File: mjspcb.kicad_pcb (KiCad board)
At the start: 2 copper layers, 83.3 x 40.1 mm, 77 parts, among them P1 3xAAA battery, P1** 2.7 - 6.0 VDC, P2 GND GND Vin RxD TxD RST, P3 HTU21D, P4 GPS, P5 rain, P6 light, P7 moist, P8 perfboard breakout, Q1 STU60N3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

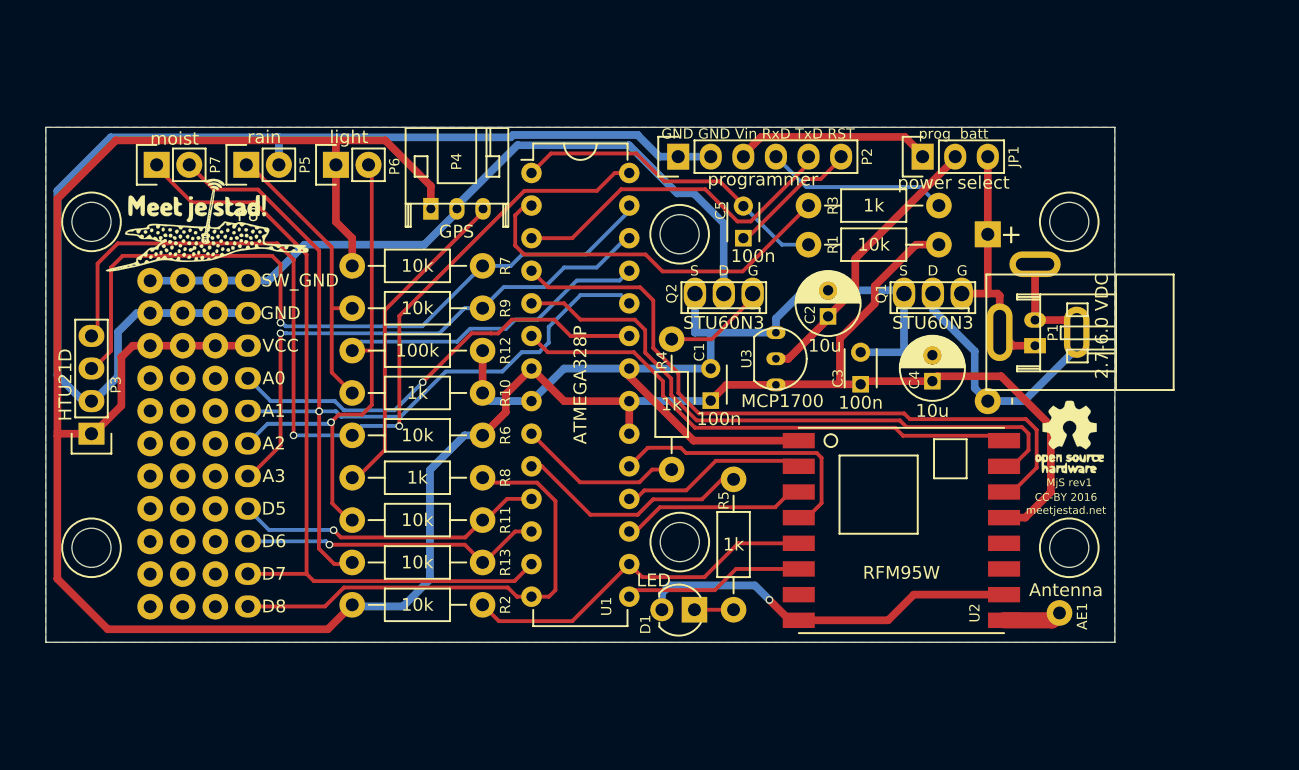
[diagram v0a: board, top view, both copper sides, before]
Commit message: Revision 2 of Meet je stad PCB
*added reset header
*changed pinout of I2C breakout to accomodate Sparkfun Si7021
*various minor other modifications
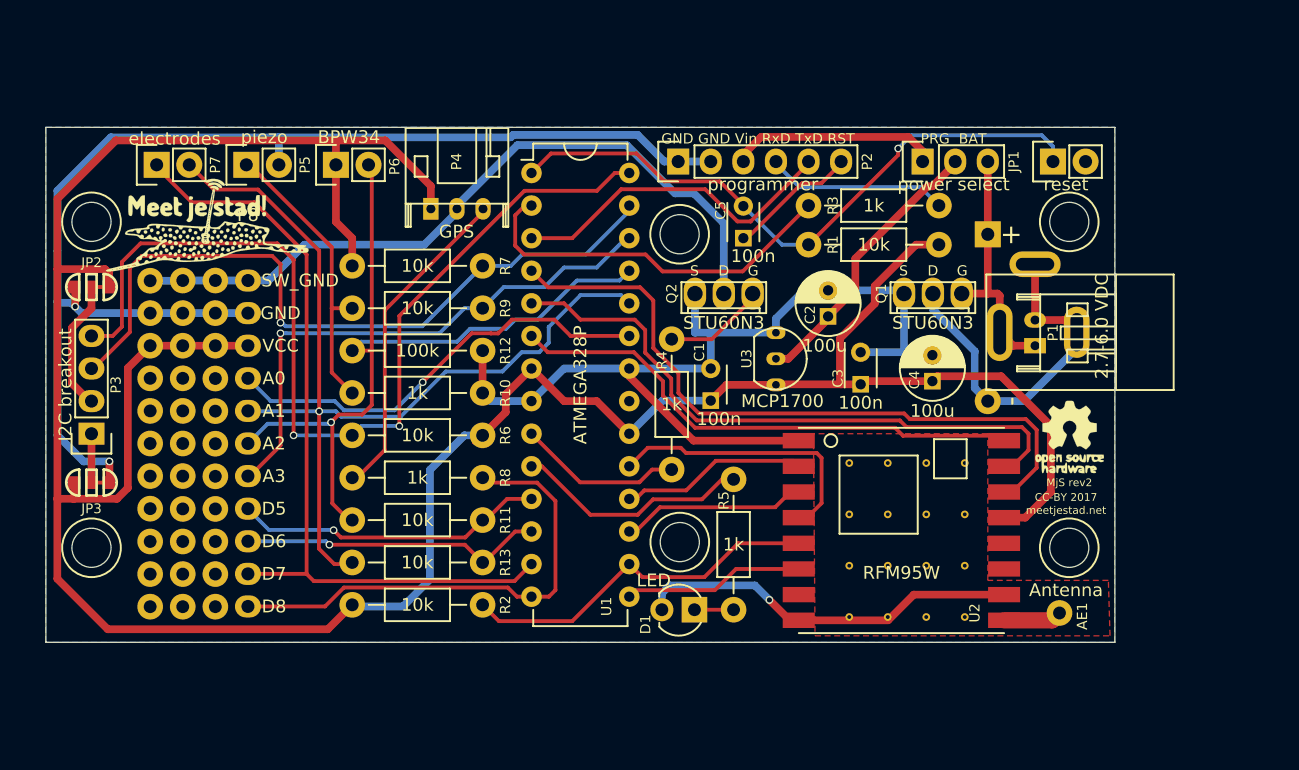
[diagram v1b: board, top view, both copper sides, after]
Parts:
- added JP2: V1, meetjestad:SOLDER-JUMPER_2-WAY-CLOSED, F.Cu at (139.7, 113.0)
- added JP3: V2, meetjestad:SOLDER-JUMPER_2-WAY-CLOSED, F.Cu at (139.7, 128.3)
- added P9: reset, meetjestad:Socket_Strip_Straight_1x02, F.Cu at (214.6, 103.3)
- added REF**: via-0.6mm, meetjestad:via-0.6mm, F.Cu at (207.8, 138.7)
- added REF**: via-0.6mm, meetjestad:via-0.6mm, F.Cu at (204.8, 130.7)
- added REF**: via-0.6mm, meetjestad:via-0.6mm, F.Cu at (201.8, 130.7)
- added REF**: via-0.6mm, meetjestad:via-0.6mm, F.Cu at (198.8, 130.7)
- added REF**: via-0.6mm, meetjestad:via-0.6mm, F.Cu at (207.8, 126.7)
- added REF**: via-0.6mm, meetjestad:via-0.6mm, F.Cu at (204.8, 126.7)
- added REF**: via-0.6mm, meetjestad:via-0.6mm, F.Cu at (201.8, 126.7)
- added REF**: via-0.6mm, meetjestad:via-0.6mm, F.Cu at (198.8, 126.7)
- added REF**: via-0.6mm, meetjestad:via-0.6mm, F.Cu at (204.8, 138.7)
- added REF**: via-0.6mm, meetjestad:via-0.6mm, F.Cu at (201.8, 138.7)
- added REF**: via-0.6mm, meetjestad:via-0.6mm, F.Cu at (198.8, 138.7)
- added REF**: via-0.6mm, meetjestad:via-0.6mm, F.Cu at (207.8, 134.7)
- added REF**: via-0.6mm, meetjestad:via-0.6mm, F.Cu at (204.8, 134.7)
- added REF**: via-0.6mm, meetjestad:via-0.6mm, F.Cu at (201.8, 134.7)
- added REF**: via-0.6mm, meetjestad:via-0.6mm, F.Cu at (198.8, 134.7)
- added REF**: via-0.6mm, meetjestad:via-0.6mm, F.Cu at (207.8, 130.7)
- C2, C4: value 10u -> 100u
- JP1: value prog batt -> PRG BAT
- P1: value 3xAAA battery -> 2.7 - 6.0 VDC
- P3: value HTU21D -> I2C breakout
- P5: value rain -> piezo
- P6: value light -> BPW34
- P7: value moist -> electrodes
- moved JP1 0.38 mm to (204.5, 103.3)
- moved P2 0.38 mm to (185.4, 103.3)
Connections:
- P3 pad 1: VCC -> GND
- P3 pad 2: GND -> VCC
- U1 pad 21: VCC -> Net-(U1-Pad21)
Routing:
- net RST: track 25.4 -> 49.9 mm, vias 0 -> 1
- net VCC: track 221.7 -> 244.6 mm
- net GND: track 195.0 -> 208.6 mm, vias 1 -> 3
- net Net-(JP1-Pad3): track 22.3 -> 21.0 mm
- net Net-(C2-Pad1): track 22.5 -> 21.6 mm
- net SDA: track 58.6 -> 57.7 mm
- added copper zone on F.Cu, net GND
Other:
- board text added: "CC-BY 2017"
- board text added: "MjS rev2"
- board text removed: "CC-BY 2016"
- board text removed: "MjS rev1"

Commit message: Add DC plug and Lipo connector to schematic
These were in the board layout, but not in the schematic. This adds them
to the schematic, and sets the appropriate references in the layouted
footprints.

Note that the DC plug symbol has a different pin numbering than the
footprint currently in use, but the symbol does match the footprint set
in the schematic, so this should work out when the netlist is re-read in
the future.
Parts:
- renumbered DC to DC1, P1** to P10
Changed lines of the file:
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@@
     (at 213.233 116.60124 90)
     (descr "JST PH series connector, S2B-PH-KL")
-    (fp_text reference P1** (at 3.31724 3.302 90) (layer F.SilkS) hide
+    (fp_text reference P10 (at 3.31724 3.302 90) (layer F.SilkS) hide
       (effects (font (size 0.8 0.8) (thickness 0.1)))
     )
@@
     (at 216.73312 116.55298 90)
     (descr "Socket, DC power supply")
-    (fp_text reference DC (at 0 6.27888 90) (layer F.SilkS) hide
+    (fp_text reference DC1 (at 0 6.27888 90) (layer F.SilkS) hide
       (effects (font (size 1 1) (thickness 0.15)))
     )

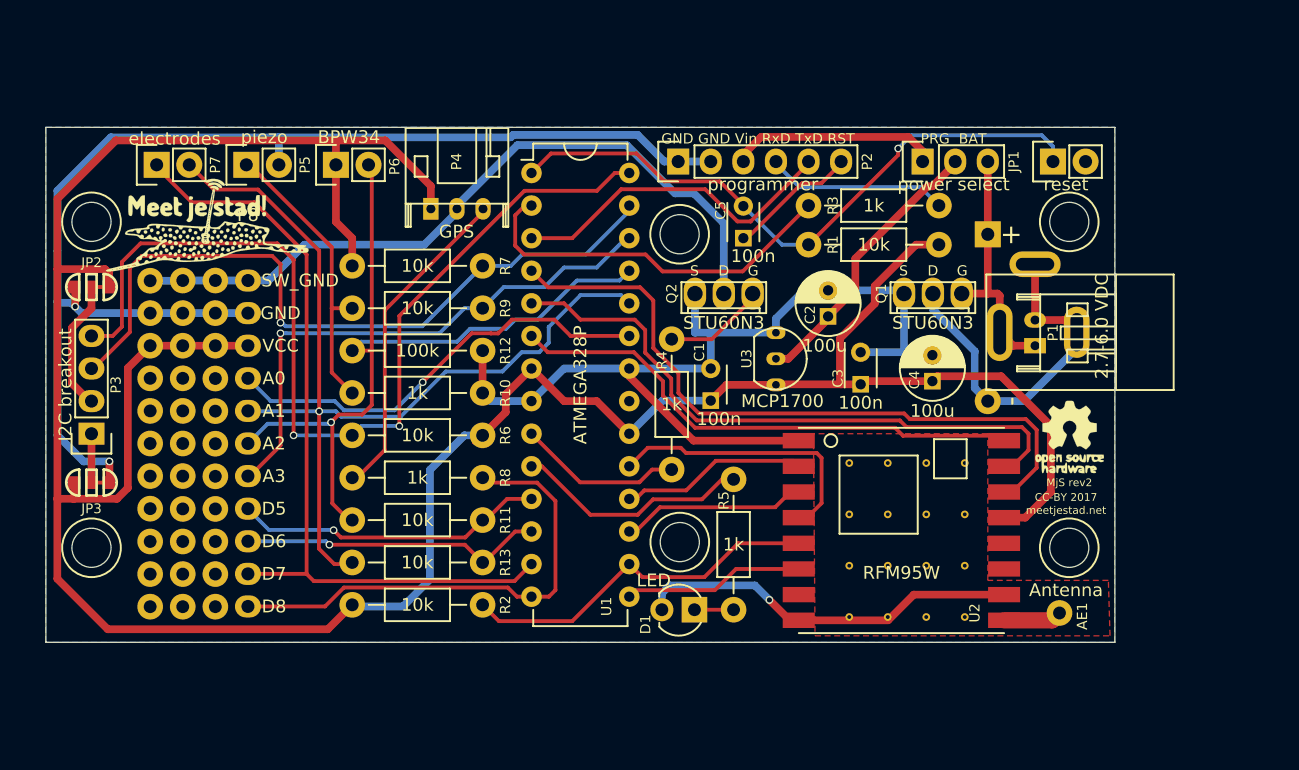
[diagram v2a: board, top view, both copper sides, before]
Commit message: Convert board layout to KiCad 5
This replaces all footprints with new versions from KiCad 5. Some
positions and labeling as changed, so this updates everything to match
the original layout for the most part. Some footprints (barrel jack,
regulator, battery holder, solder jumpers, perfboard "connector") are
slightly different. In particualr the battery holde slightly changes the
mounting hole position and size, so this might need to be changed back
later.

The only footprints that are still used from the project library are the
logo, all others are removed. All components are also in the schematic,
except for the perfboard individiual pins (which also do not have any
external footprint they refer to).

The GPS connector footprint has holes that are slightly (0.05mm) bigger,
which should make it easier to fit the connector.
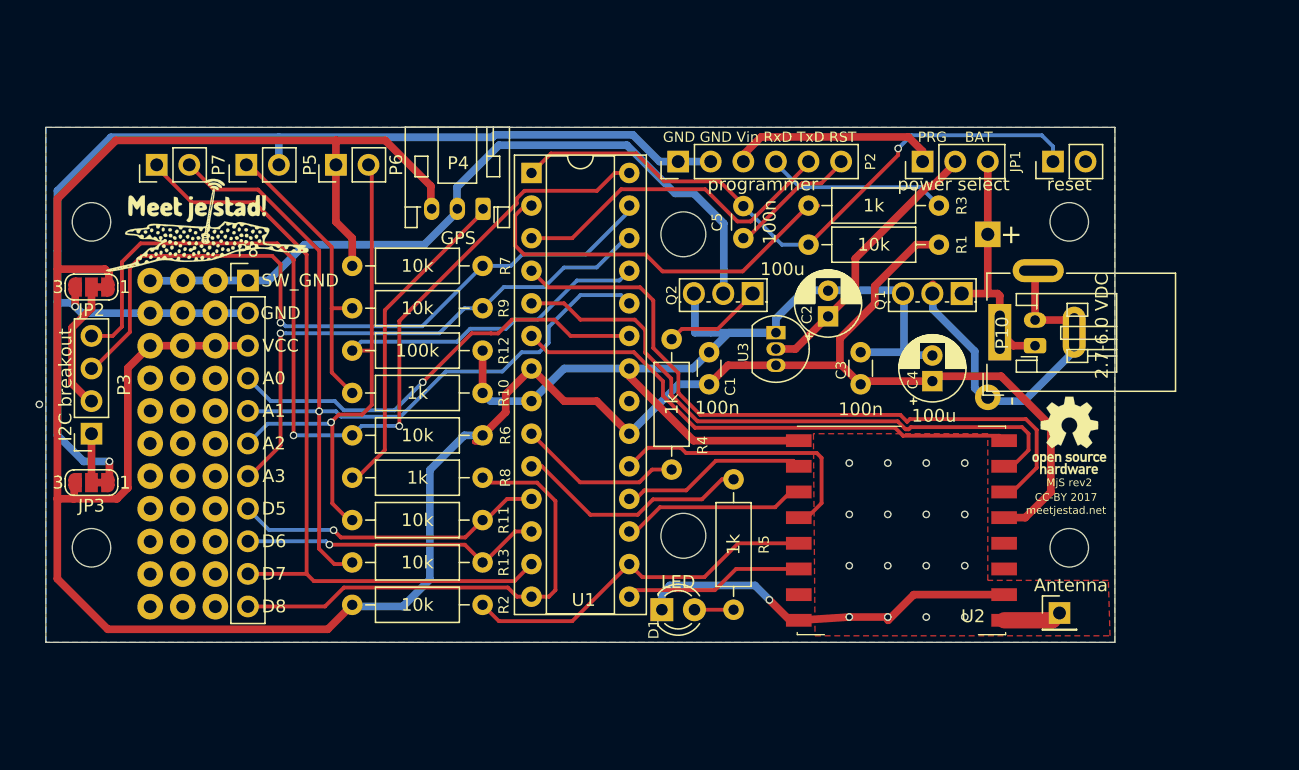
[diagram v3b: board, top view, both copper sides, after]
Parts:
- removed the ? at (185.5, 132.9)
- removed the ? at (185.5, 108.9)
- removed REF** (x16): via-0.6mm, meetjestad:via-0.6mm
- AE1: footprint meetjestad:1pin -> Connector_PinHeader_2.54mm:PinHeader_1x01_P2.54mm_Vertical
- C1, C3, C5: footprint meetjestad:C_Disc_D3_P2.5 -> Capacitor_THT:C_Disc_D3.0mm_W1.6mm_P2.50mm
- C2: footprint meetjestad:C_Radial_D5_L11_P2 -> Capacitor_THT:CP_Radial_D5.0mm_P2.00mm
- C4: footprint C_Radial_D5_L11_P2 -> Capacitor_THT:CP_Radial_D5.0mm_P2.00mm
- D1: footprint LED-3MM -> LED_THT:LED_D3.0mm
- DC1: value P1* -> 2.7 - 6.0 VDC; footprint dc_socket -> Connector_BarrelJack:BarrelJack_Wuerth_6941xx301002
- H1, H2, H3, H4: renamed from ?; value (none) -> MountingHole; footprint Connect:1pin -> MountingHole:MountingHole_3mm
- JP1: value PRG BAT -> power select; footprint meetjestad:Pin_Header_Straight_1x03 -> Connector_PinHeader_2.54mm:PinHeader_1x03_P2.54mm_Vertical
- JP2, JP3: footprint meetjestad:SOLDER-JUMPER_2-WAY-CLOSED -> Jumper:SolderJumper-3_P1.3mm_Bridged12_RoundedPad1.0x1.5mm_NumberLabels
- LOGO1: renamed from G2; value OSHW logo -> Open source hardware; footprint meetjestad:oshw -> Symbol:OSHW-Logo_5.7x6mm_SilkScreen
- LOGO2: renamed from G1; value MjS logo -> MJS Logo
- P1: value 2.7 - 6.0 VDC -> Batteries; footprint Batterypack3xAAA -> Battery:BatteryHolder_Keystone_2479_3xAAA
- P10: value 2.7 - 6.0 VDC -> Lipo; footprint s2b-ph-kl -> Connector_JST:JST_PH_S2B-PH-K_1x02_P2.00mm_Horizontal
- P2: value GND GND Vin RxD TxD RST -> serial breakout; footprint meetjestad:Pin_Header_Straight_1x06 -> Connector_PinHeader_2.54mm:PinHeader_1x06_P2.54mm_Vertical
- P3: footprint meetjestad:Socket_Strip_Straight_1x04 -> Connector_PinSocket_2.54mm:PinSocket_1x04_P2.54mm_Vertical
- P4: footprint s3b-ph-kl -> Connector_JST:JST_PH_S3B-PH-K_1x03_P2.00mm_Horizontal
- P5, P6, P7, P9: footprint meetjestad:Socket_Strip_Straight_1x02 -> Connector_PinHeader_2.54mm:PinHeader_1x02_P2.54mm_Vertical
- P8: footprint Perf_board_connecttion_1x11 -> Connector_PinHeader_2.54mm:PinHeader_1x11_P2.54mm_Vertical
- Q1, Q2: value STU60N3 -> STU60N3LH5; footprint meetjestad:ipak_std -> Package_TO_SOT_THT:TO-251-3_Vertical
- R1, R10, R11, R12, R13, R2, R3, R4, R5, R6, R7, R8, R9: footprint meetjestad:Resistor_Horizontal_RM10mm -> Resistor_THT:R_Axial_DIN0207_L6.3mm_D2.5mm_P10.16mm_Horizontal
- U1: footprint meetjestad:DIP-28_W7.62mm -> Package_DIP:DIP-28_W7.62mm_Socket
- U2: footprint RFM95W -> RF_Module:HOPERF_RFM9XW_SMD
- U3: value MCP1700 -> MCP1700-3302; footprint TO-92_Inline_Narrow_Oval -> Package_TO_SOT_THT:TO-92_Inline
- moved P1 31.1 mm to (209.6, 108.9)
- moved DC1 6.25 mm to (210.5, 116.6)
- moved R1 5.08 mm to (205.7, 109.7)
- moved R3 5.08 mm to (205.7, 106.7)
- moved R4 5.08 mm to (184.9, 117.1)
- moved R5 5.08 mm to (189.7, 128.0)
- moved R6 5.08 mm to (170.2, 124.6)
- moved R10 5.08 mm to (160.0, 121.3)
- moved R11 5.08 mm to (160.0, 131.2)
- moved R12 5.08 mm to (160.0, 118.0)
- moved R13 5.08 mm to (160.0, 134.5)
- moved R2 5.08 mm to (160.0, 137.8)
- moved R7 5.08 mm to (160.0, 111.4)
- moved R8 5.08 mm to (160.0, 127.9)
- moved R9 5.08 mm to (160.0, 114.7)
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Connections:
- net Net-(C2-Pad1) renamed VIN
- net Net-(R2-Pad2) renamed D10
- net Net-(U1-Pad15) renamed D9
- net Net-(U1-Pad17) renamed MOSI
- net Net-(U1-Pad18) renamed MISO
- net Net-(U1-Pad19) renamed SCK
- net Net-(U1-Pad4) renamed D2
- net Net-(U1-Pad5) renamed D3
- net Net-(U1-Pad6) renamed D4
- DC1 pad 1: Net-(P1-Pad1) -> +BATT
- DC1 pad 2: Net-(P1-Pad1) -> -BATT
- DC1 pad 3: Net-(JP1-Pad3) -> -BATT
- JP1 pad 3: Net-(JP1-Pad3) -> +BATT
- JP2 pad 2: GND -> Net-(JP2-Pad2)
- JP3 pad 2: VCC -> Net-(JP3-Pad2)
- P1 pad 1: Net-(P1-Pad1) -> +BATT
- P1 pad 2: Net-(JP1-Pad3) -> -BATT
- P10 pad 1: Net-(JP1-Pad3) -> +BATT
- P10 pad 2: Net-(P1-Pad1) -> -BATT
- P3 pad 1: GND -> Net-(JP3-Pad2)
- P3 pad 2: VCC -> Net-(JP2-Pad2)
- P4 pad 1: VCC -> Net-(P4-Pad1)
- P4 pad 3: Net-(P4-Pad3) -> VCC
- Q1 pad 1: Net-(JP1-Pad3) -> +BATT
- Q1 pad 2: Net-(P1-Pad1) -> -BATT
- R8 pad 1: Net-(P4-Pad3) -> Net-(P4-Pad1)
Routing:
- net Net-(P1-Pad1): track 31.5 -> 0.00 mm
- net -BATT: track 0.00 -> 31.5 mm
- net Net-(P4-Pad3): track 25.6 -> 0.00 mm
- net Net-(P4-Pad1): track 0.00 -> 25.6 mm
- net Net-(JP1-Pad3): track 21.0 -> 0.00 mm
- net +BATT: track 0.00 -> 21.0 mm
- net VCC: track 244.6 -> 232.8 mm
- net Net-(JP2-Pad2): track 0.00 -> 10.2 mm
- net Net-(JP3-Pad2): track 0.00 -> 3.81 mm
- net GND: track 208.6 -> 207.1 mm, vias 3 -> 19
- net Net-(Q2-Pad1): track 9.06 -> 7.81 mm
- net SW_GND: track 57.4 -> 58.2 mm
- net (no net): vias 0 -> 1
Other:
- board text added: "GND GND Vin RxD TxD RST"
- board text added: "I2C breakout"
- board text added: "PRG BAT"
